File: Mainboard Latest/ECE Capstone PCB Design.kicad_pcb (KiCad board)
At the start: 2 copper layers, 114.9 x 66.9 mm, 72 parts, among them J1 1053131105, J2 1053131105, J3 Conn_01x40_Socket, U1 MCP2518FDT-H/SL, U2 MCP2542FD-E/SN, U5 TPS562201, U6 TPS61165DBV, U7 TPS562201

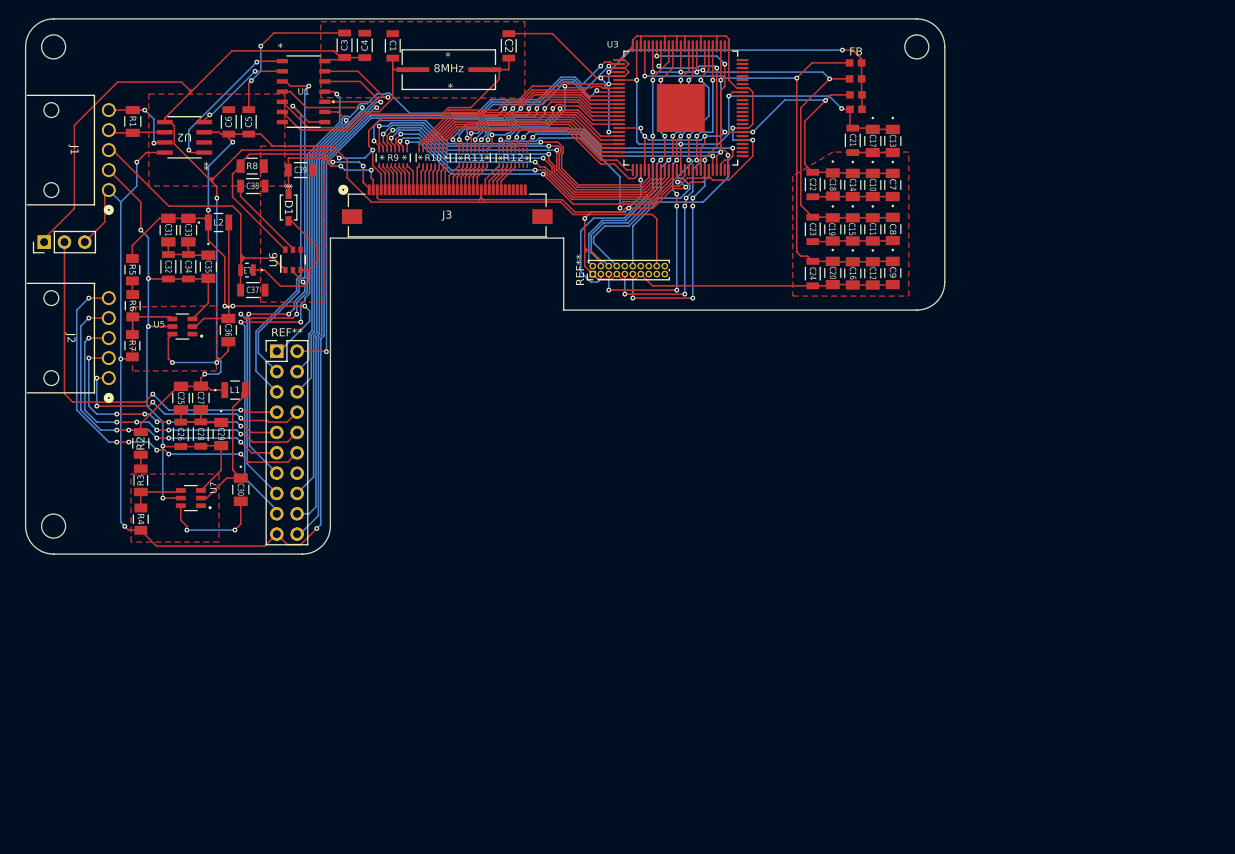
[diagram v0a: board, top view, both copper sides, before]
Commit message: Added the first daughter board. Added a model of the pi
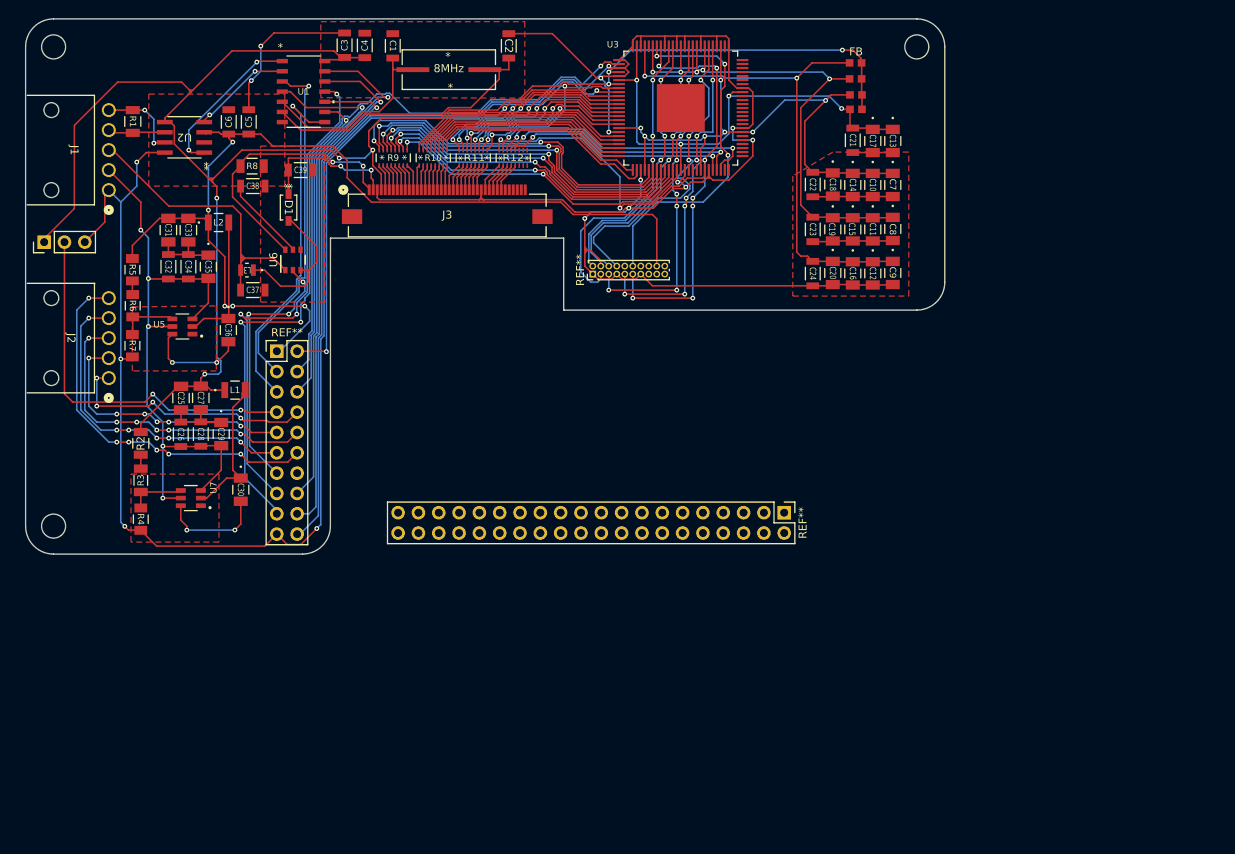
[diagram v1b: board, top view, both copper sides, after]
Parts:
- added REF**: PinHeader_2x20_P2.54mm_Vertical, Connector_PinHeader_2.54mm:PinHeader_2x20_P2.54mm_Vertical, F.Cu at (217.4, 108.8)

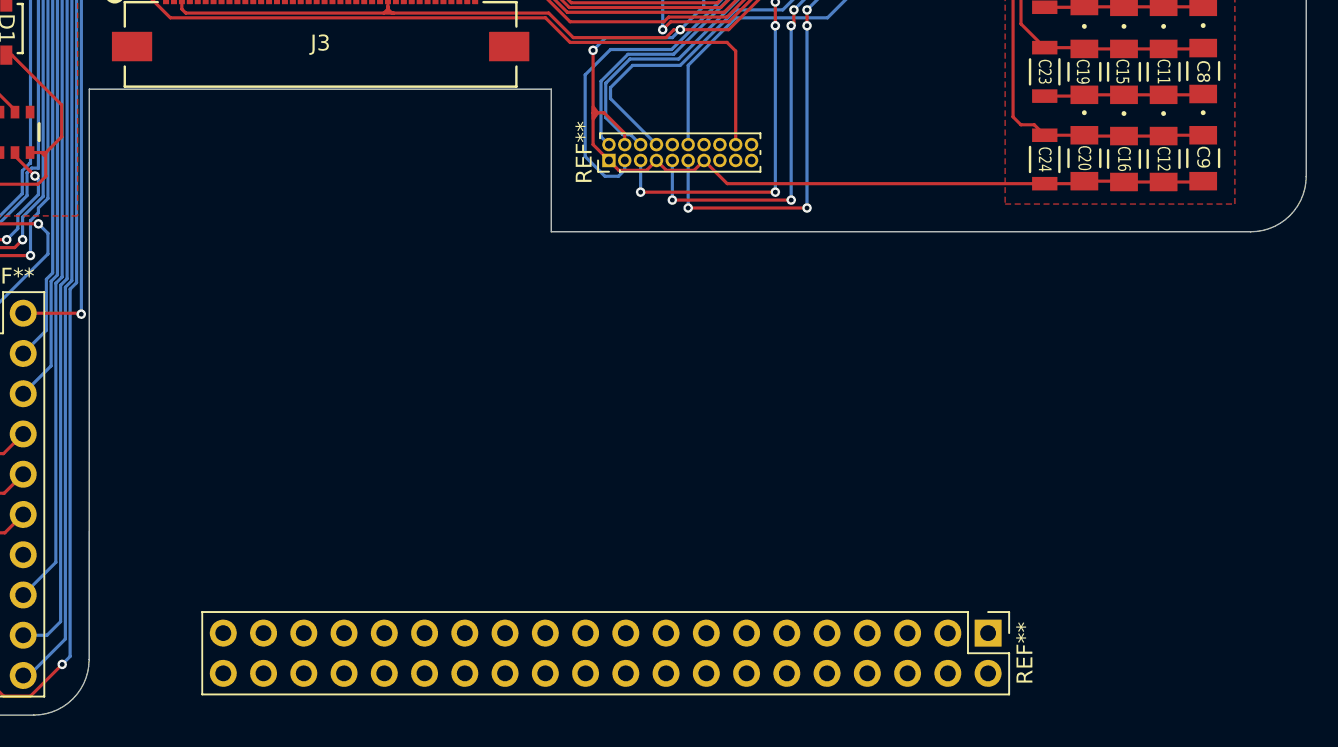
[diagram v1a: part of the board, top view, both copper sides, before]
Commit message: Completed pi daughter board. Dimensions should be accurate to 0.025mm. Placed it with the mainboard in such a way that it is configured for paneling
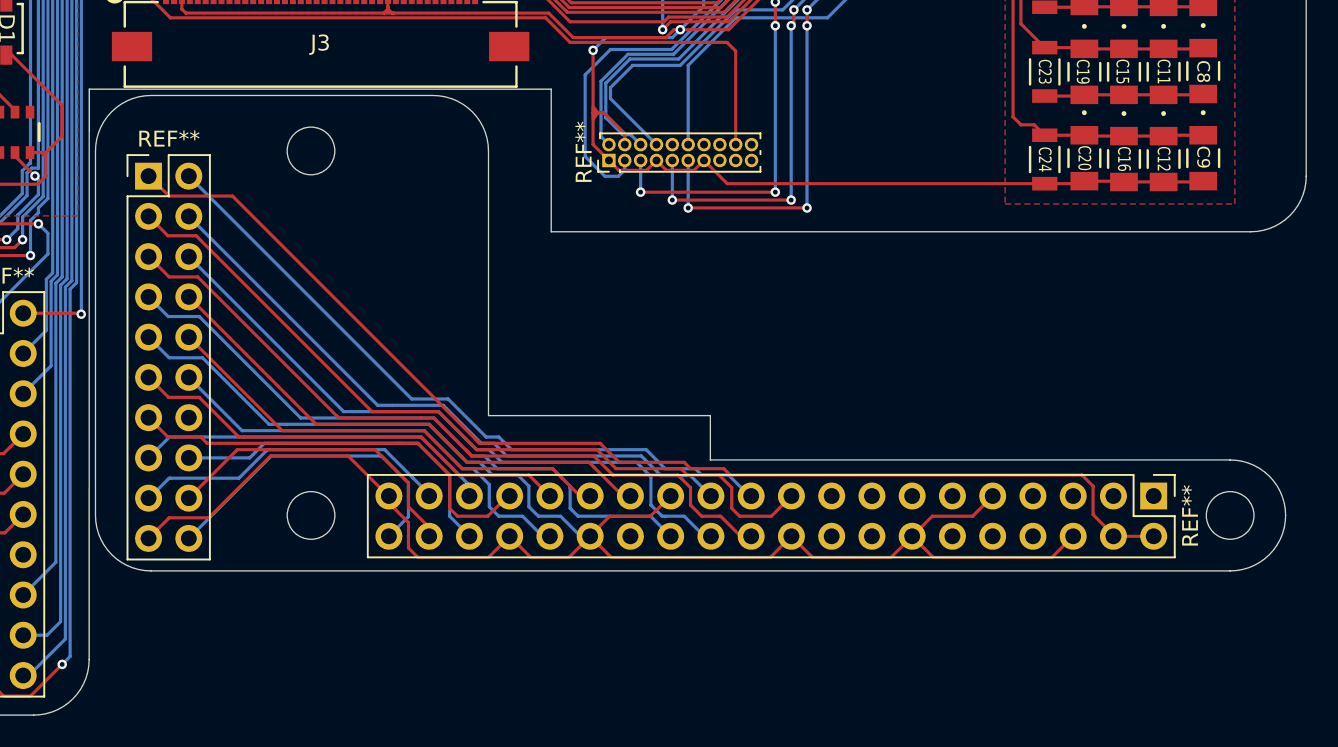
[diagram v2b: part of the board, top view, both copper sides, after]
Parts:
- added REF**: PinHeader_2x10_P2.54mm_Vertical, Connector_PinHeader_2.54mm:PinHeader_2x10_P2.54mm_Vertical, F.Cu at (164.4, 80.0)
- moved REF** 13.6 mm to (227.9, 100.2)
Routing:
- net /GND: track 418.8 -> 660.1 mm
- net (no net): track 0.00 -> 163.1 mm
- net +5V: track 123.0 -> 197.8 mm
- net /Rasberry PI (clock output): track 43.1 -> 93.3 mm
- net /Rasberry PI (TX interupt active low): track 44.4 -> 91.3 mm
- net /Rasberry PI (SPI clock input): track 64.8 -> 104.9 mm
- net unconnected-(J2-Pad1): track 31.8 -> 64.9 mm
- net Net-(J3-Pad7): track 43.6 -> 73.0 mm
- net /PWM: track 33.5 -> 60.6 mm
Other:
- outline, holes or cut-outs redrawn

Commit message: Laid out HDMI daughter board. HDMI interconnect not finished yet. Added screw hole for HDMI daughterboard. Moved the display decoder capacitors further towards the right edge of the main board and re-did the traces to the ferrite beads in order to make room for another screw hole with proper screw mounting margins.
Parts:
- added REF**: PinHeader_2x10_P1.00mm_Vertical, Connector_PinHeader_1.00mm:PinHeader_2x10_P1.00mm_Vertical, F.Cu at (177.8, 138.9)
- moved REF** 4.75 mm to (227.9, 104.9)
- moved REF** 4.75 mm to (164.5, 84.7)
- moved C18 2.22 mm to (225.7, 68.1)
- moved C22 2.22 mm to (223.2, 68.1)
- moved C21 2.22 mm to (228.2, 62.6)
- moved C10 2.22 mm to (230.7, 68.2)
- moved C11 2.22 mm to (230.7, 73.7)
- moved C12 2.22 mm to (230.7, 79.2)
- moved C13 2.22 mm to (233.2, 62.7)
- moved C14 2.22 mm to (228.2, 68.2)
- moved C15 2.22 mm to (228.2, 73.7)
- moved C16 2.22 mm to (228.2, 79.2)
- moved C17 2.22 mm to (230.7, 62.7)
- moved C19 2.22 mm to (225.7, 73.7)
- moved C20 2.22 mm to (225.7, 79.2)
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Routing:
- net /GND: track 660.1 -> 662.6 mm
- net Net-(U3-PVDD): track 64.4 -> 66.0 mm
- net Net-(U3-DVDD): track 59.3 -> 60.6 mm
- net Net-(U3-AVDD): track 67.3 -> 66.7 mm
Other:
- board size 114.9 x 66.9 mm -> 114.9 x 96.4 mm

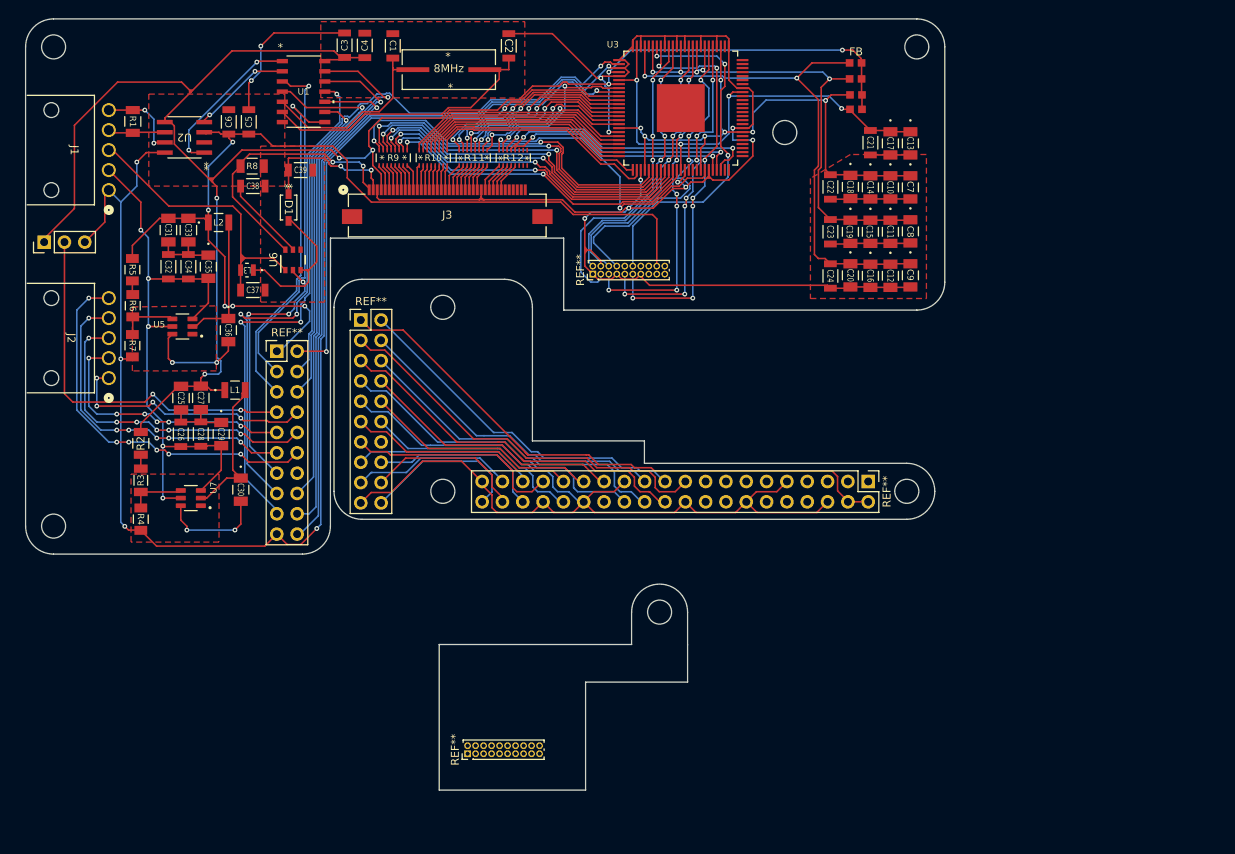
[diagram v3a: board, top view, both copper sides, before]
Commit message: Completed mainboard redesign and all daughter boards
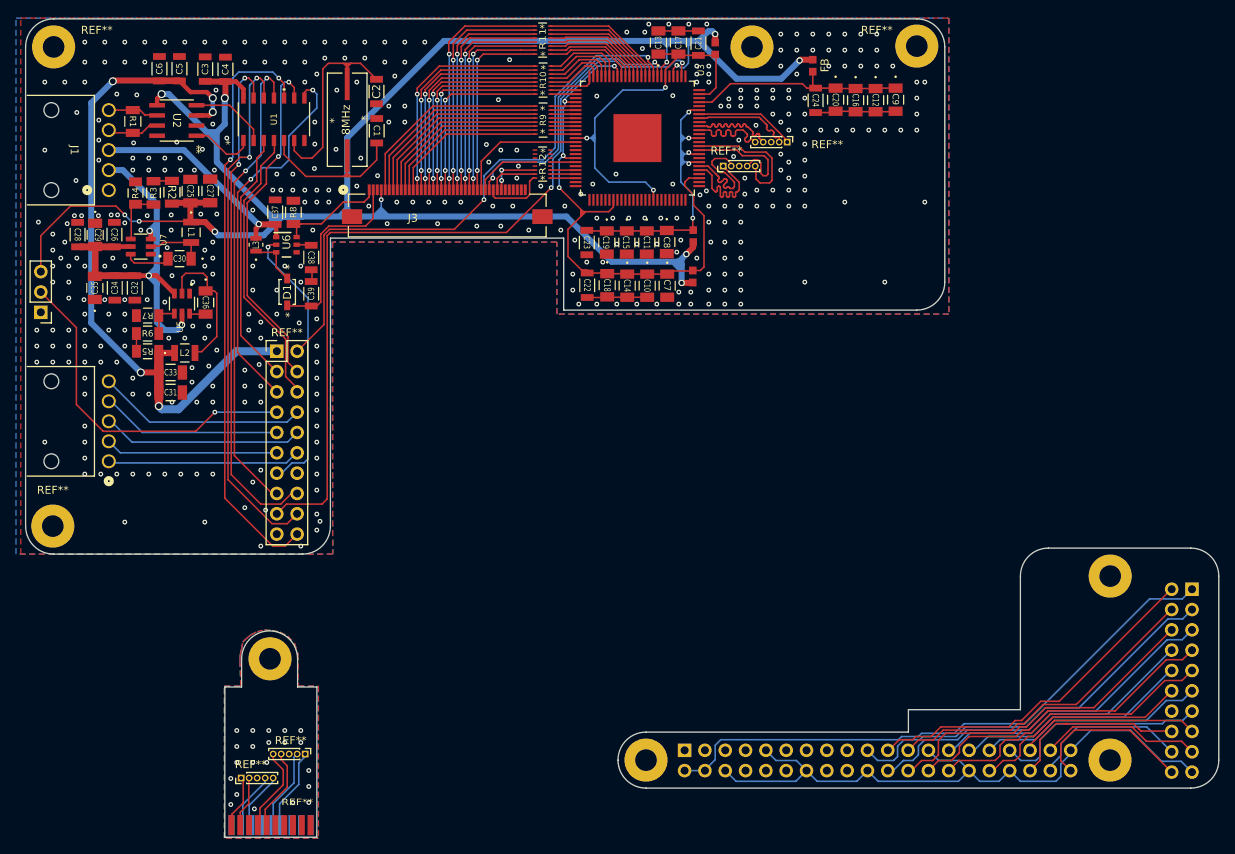
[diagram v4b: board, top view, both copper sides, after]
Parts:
- removed the REF** at (177.8, 138.9)
- removed the REF** at (193.5, 79.0)
- added ?: , , F.Cu at (153.1, 127.1)
- added ?: , , F.Cu at (213.4, 50.6)
- added ?: , , B.Cu at (258.1, 139.8)
- added ?: , , B.Cu at (200.1, 139.8)
- added ?: , , B.Cu at (258.2, 116.8)
- added REF**: PinHeader_1x05_P1.00mm_Vertical, Connector_PinHeader_1.00mm:PinHeader_1x05_P1.00mm_Vertical, F.Cu at (217.8, 62.5)
- added REF**: PinHeader_1x05_P1.00mm_Vertical, Connector_PinHeader_1.00mm:PinHeader_1x05_P1.00mm_Vertical, F.Cu at (149.6, 142.0)
- added REF**: MountingHole_2.7mm_M2.5_Pad, MountingHole:MountingHole_2.7mm_M2.5_Pad, F.Cu at (126.1, 50.6)
- added REF**: MULTICOMP_60S019P-301N-B1-FEC, Connector_Video:Mini HDMI breakout, F.Cu at (153.2, 151.5)
- added REF**: PinHeader_1x05_P1.00mm_Vertical, Connector_PinHeader_1.00mm:PinHeader_1x05_P1.00mm_Vertical, F.Cu at (157.6, 139.0)
- added REF**: MountingHole_2.7mm_M2.5_Pad, MountingHole:MountingHole_2.7mm_M2.5_Pad, F.Cu at (234.0, 50.5)
- added REF**: PinHeader_1x05_P1.00mm_Vertical, Connector_PinHeader_1.00mm:PinHeader_1x05_P1.00mm_Vertical, F.Cu at (209.8, 65.5)
- added REF**: MountingHole_2.7mm_M2.5_Pad, MountingHole:MountingHole_2.7mm_M2.5_Pad, F.Cu at (126.0, 110.5)
- REF** (x2): moved to B.Cu
- moved REF** 109.2 mm to (268.4, 118.4), turned to 180 degrees
- moved R4 40.8 mm to (136.3, 68.9), turned to 90 degrees
- moved REF** 40.7 mm to (205.0, 138.5)
- moved R3 36.0 mm to (138.6, 68.8)
- moved C13 33.9 mm to (201.7, 50.1), turned to 90 degrees
- moved C10 32.8 mm to (200.3, 80.4)
- moved C14 32.8 mm to (197.8, 80.4)
- moved C18 32.8 mm to (195.3, 80.4)
- moved C22 32.8 mm to (192.8, 80.4)
- moved C7 32.8 mm to (202.8, 80.4)
- moved U7 32.1 mm to (137.0, 75.6)
- moved R2 31.6 mm to (140.9, 68.8), turned to -90 degrees
- moved FB1 30.5 mm to (206.0, 79.3), turned to 90 degrees
- moved C11 30.5 mm to (200.2, 75.1)
- moved C15 30.5 mm to (197.8, 75.1)
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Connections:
- C25 pad 1: +3.3V -> /GND
- C26 pad 1: +3.3V -> /GND
- C27 pad 1: +3.3V -> /GND
- C28 pad 1: +3.3V -> /GND
- C29 pad 1: +3.3V -> /GND
- C31 pad 2: +3.3V -> /GND
- C32 pad 1: +3.3V -> /GND
- C33 pad 2: +3.3V -> /GND
- C34 pad 1: +3.3V -> /GND
- C35 pad 1: +3.3V -> /GND
- J1 pad 4: /CAN Bus connection L -> /CAN Bus connection H
- J1 pad 5: /CAN Bus connection H -> /CAN Bus connection L
- J2 pad 1: unconnected-(J2-Pad1) -> BT4
- J2 pad 2: Net-(J3-Pad6) -> BT3
- J2 pad 3: Net-(J3-Pad7) -> BT2
- J2 pad 4: Net-(J3-Pad8) -> BT1
- J2 pad 5: Net-(J3-Pad9) -> BT0
- J3 pad 10: Net-(J3-Pad10) -> RO5
- J3 pad 11: Net-(J3-Pad11) -> RO6
- J3 pad 12: Net-(J3-Pad12) -> RO7
- J3 pad 13: Net-(J3-Pad13) -> GO0
- J3 pad 14: Net-(J3-Pad14) -> GO1
- J3 pad 15: Net-(J3-Pad15) -> GO2
- J3 pad 16: Net-(J3-Pad16) -> GO3
- J3 pad 17: Net-(J3-Pad17) -> GO4
- J3 pad 18: Net-(J3-Pad18) -> GO5
- J3 pad 19: Net-(J3-Pad19) -> GO6
- J3 pad 20: Net-(J3-Pad20) -> GO7
- J3 pad 21: Net-(J3-Pad21) -> BO0
- J3 pad 22: Net-(J3-Pad22) -> BO1
- J3 pad 23: Net-(J3-Pad23) -> BO2
- J3 pad 24: Net-(J3-Pad24) -> BO3
- J3 pad 25: Net-(J3-Pad25) -> BO4
- J3 pad 26: Net-(J3-Pad26) -> BO5
- J3 pad 27: Net-(J3-Pad27) -> BO6
- J3 pad 28: Net-(J3-Pad28) -> BO7
- J3 pad 30: /PIXCLK -> PIXCLKOO
- J3 pad 32: /HSYNC -> HSYNCO
- J3 pad 33: /VSYNC -> VSYNCO
- J3 pad 34: /DISPEN -> DISPENO
- J3 pad 5: Net-(J3-Pad5) -> /RO0
- J3 pad 6: Net-(J3-Pad6) -> RO1
- J3 pad 7: Net-(J3-Pad7) -> RO2
- J3 pad 8: Net-(J3-Pad8) -> RO3
- J3 pad 9: Net-(J3-Pad9) -> RO4
- R1 pad 1: /CAN Bus connection H -> /CAN Bus connection L
- R1 pad 2: /CAN Bus connection L -> /CAN Bus connection H
- R10 pad 1: Net-(J3-Pad13) -> /G7
- R10 pad 10: /G6 -> GO1
- R10 pad 11: /G5 -> GO2
- R10 pad 12: /G4 -> GO3
- R10 pad 13: /G3 -> GO4
- R10 pad 14: /G2 -> GO5
- R10 pad 15: /G1 -> GO6
- R10 pad 16: /G0 -> GO7
- R10 pad 2: Net-(J3-Pad14) -> /G6
- R10 pad 3: Net-(J3-Pad15) -> /G5
- R10 pad 4: Net-(J3-Pad16) -> /G4
- R10 pad 5: Net-(J3-Pad17) -> /G3
- R10 pad 6: Net-(J3-Pad18) -> /G2
- R10 pad 7: Net-(J3-Pad19) -> /G1
- R10 pad 8: Net-(J3-Pad20) -> /G0
- R10 pad 9: /G7 -> GO0
- R11 pad 1: Net-(J3-Pad21) -> /B7
- R11 pad 10: /B6 -> BO1
- R11 pad 11: /B5 -> BO2
- R11 pad 12: /B4 -> BO3
- R11 pad 13: /B3 -> BO4
- R11 pad 14: /B2 -> BO5
- R11 pad 15: /B1 -> BO6
- R11 pad 16: /B0 -> BO7
- R11 pad 2: Net-(J3-Pad22) -> /B6
- R11 pad 3: Net-(J3-Pad23) -> /B5
- R11 pad 4: Net-(J3-Pad24) -> /B4
- R11 pad 5: Net-(J3-Pad25) -> /B3
- R11 pad 6: Net-(J3-Pad26) -> /B2
- R11 pad 7: Net-(J3-Pad27) -> /B1
- R11 pad 8: Net-(J3-Pad28) -> /B0
- R11 pad 9: /B7 -> BO0
- R12 pad 1: /PIXCLK -> /HSYNC
- R12 pad 10: unconnected-(R12-Pad10) -> /GND
- R12 pad 11: unconnected-(R12-Pad11) -> /GND
- R12 pad 12: /DISPEN -> PIXCLKOO
- R12 pad 13: /VSYNC -> /GND
- R12 pad 14: /HSYNC -> DISPENO
- R12 pad 15: /ACTIVE -> VSYNCO
- R12 pad 16: /PIXCLK -> HSYNCO
- R12 pad 2: /ACTIVE -> /VSYNC
- R12 pad 3: /HSYNC -> /DISPEN
- R12 pad 4: /VSYNC -> /GND
- R12 pad 5: /DISPEN -> /PIXCLK
- R12 pad 6: unconnected-(R12-Pad6) -> /GND
- R12 pad 7: unconnected-(R12-Pad7) -> /GND
- R12 pad 8: unconnected-(R12-Pad8) -> /GND
- R12 pad 9: unconnected-(R12-Pad9) -> /GND
- R9 pad 1: Net-(J3-Pad5) -> /R7
- R9 pad 10: /R6 -> RO1
- R9 pad 11: /R5 -> RO2
- R9 pad 12: /R4 -> RO3
- R9 pad 13: /R3 -> RO4
- R9 pad 14: /R2 -> RO5
- R9 pad 15: /R1 -> RO6
- R9 pad 16: /R0 -> RO7
- R9 pad 2: Net-(J3-Pad6) -> /R6
- R9 pad 3: Net-(J3-Pad7) -> /R5
- R9 pad 4: Net-(J3-Pad8) -> /R4
- R9 pad 5: Net-(J3-Pad9) -> /R3
- R9 pad 6: Net-(J3-Pad10) -> /R2
- R9 pad 7: Net-(J3-Pad11) -> /R1
- R9 pad 8: Net-(J3-Pad12) -> /R0
- R9 pad 9: /R7 -> /RO0
- REF** pad 10: Net-(J3-Pad7) -> BT2
- REF** pad 11: Net-(J3-Pad8) -> BT3
- REF** pad 12: Net-(J3-Pad9) -> BT4
- REF** pad 8: unconnected-(J2-Pad1) -> BT0
- REF** pad 9: Net-(J3-Pad6) -> BT1
- REF** pad 14: (no net) -> D1GND
- REF** pad 19: (no net) -> D1_Raspberry_PI_(clock_output)
- REF** pad 2: (no net) -> D1+5V
- REF** pad 20: (no net) -> D1GND
- REF** pad 21: (no net) -> D1PWRON_D
- REF** pad 22: (no net) -> D1_Raspberry_PI_(TX_interupt_active_low)
- REF** pad 23: (no net) -> D1_Raspberry_PI_(RX_interupt_active_low)
- REF** pad 24: (no net) -> D1_Raspberry_PI_(interupt_active_low)
- REF** pad 25: (no net) -> D1GND
- REF** pad 26: (no net) -> D1_Dev_pin
- REF** pad 27: (no net) -> D1_BTN0
- REF** pad 28: (no net) -> D1_BTN1
- REF** pad 29: (no net) -> D1_BTN2
- REF** pad 30: (no net) -> D1GND
- REF** pad 31: (no net) -> D1_BTN3
- REF** pad 32: (no net) -> D1_BTN4
- REF** pad 33: (no net) -> D1_PWM
- REF** pad 34: (no net) -> D1GND
- REF** pad 35: (no net) -> D1_Raspberry_PI_(SPI_Input)
- REF** pad 36: (no net) -> D1_Raspberry_PI_(chip_select)
- REF** pad 37: (no net) -> D1_PWRON
- REF** pad 38: (no net) -> D1_Raspberry_PI_(SPI_output)
- REF** pad 39: (no net) -> D1GND
- REF** pad 4: (no net) -> D1+5V
- REF** pad 40: (no net) -> D1_Raspberry_PI_(SPI_clock_input)
- REF** pad 6: (no net) -> D1GND
- REF** pad 9: (no net) -> D1GND
- REF** pad 1: (no net) -> D1+5V
- REF** pad 10: (no net) -> D1_BTN2
- REF** pad 11: (no net) -> D1_BTN3
- REF** pad 12: (no net) -> D1_BTN4
- REF** pad 13: (no net) -> D1_PWM
- REF** pad 15: (no net) -> D1_Raspberry_PI_(SPI_Input)
- REF** pad 16: (no net) -> D1_Raspberry_PI_(chip_select)
- REF** pad 17: (no net) -> D1_PWRON
- REF** pad 18: (no net) -> D1_Raspberry_PI_(SPI_output)
- REF** pad 19: (no net) -> D1GND
- REF** pad 2: (no net) -> D1PWRON_D
- REF** pad 20: (no net) -> D1_Raspberry_PI_(SPI_clock_input)
- REF** pad 3: (no net) -> D1_Raspberry_PI_(clock_output)
- REF** pad 4: (no net) -> D1_Raspberry_PI_(RX_interupt_active_low)
- REF** pad 5: (no net) -> D1_Raspberry_PI_(TX_interupt_active_low)
- REF** pad 6: (no net) -> D1_Raspberry_PI_(interupt_active_low)
- REF** pad 7: (no net) -> D1_Dev_pin
- REF** pad 8: (no net) -> D1_BTN0
- REF** pad 9: (no net) -> D1_BTN1
- REF** pad 1: +3.3V -> /GND
- REF** pad 3: /GND -> +3.3V
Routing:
- net /GND: track 662.6 -> 41.3 mm, vias 16 -> 387
- net (no net): track 163.1 -> 0.00 mm
- net +5V: track 197.8 -> 89.1 mm
- net D1GND: track 0.00 -> 82.2 mm
- net D1+5V: track 0.00 -> 74.3 mm
- net Net-(J3-Pad7): track 73.0 -> 0.00 mm, vias 6 -> 0
- net unconnected-(J2-Pad1): track 64.9 -> 0.00 mm, vias 4 -> 0
- net /Rasberry PI (clock output): track 93.3 -> 32.3 mm, vias 1 -> 0
- net Net-(J3-Pad9): track 51.0 -> 0.00 mm, vias 6 -> 0
- net D1_Raspberry_PI_(clock_output): track 0.00 -> 50.2 mm
- net D1_Raspberry_PI_(TX_interupt_active_low): track 0.00 -> 46.4 mm
- net Net-(J3-Pad8): track 44.3 -> 0.00 mm, vias 6 -> 0
- net D1PWRON_D: track 0.00 -> 44.1 mm
- net /Rasberry PI (TX interupt active low): track 91.3 -> 47.3 mm, vias 1 -> 2
- net /R0: track 44.6 -> 3.11 mm, vias 2 -> 0
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- added copper zone on B.Cu, net /GND
- added copper zone on B.Cu, net DGND
- added copper zone on F.Cu, net DGND
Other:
- board size 114.9 x 96.4 mm -> 149.1 x 102.3 mm
